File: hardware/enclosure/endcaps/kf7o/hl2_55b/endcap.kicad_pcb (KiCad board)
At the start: 2 copper layers, 106 x 55 mm, 46 parts, among them J2 Male Header, J3 Male Header, J4 Fan, Q1 DTC144E, Q2 IRLML6402, Q3 MULTIFET, Q4 MULTIFET, Q5 MULTIFET, Q6 MULTIFET, Q7 MULTIFET, U1 ACPL-M21L-000E

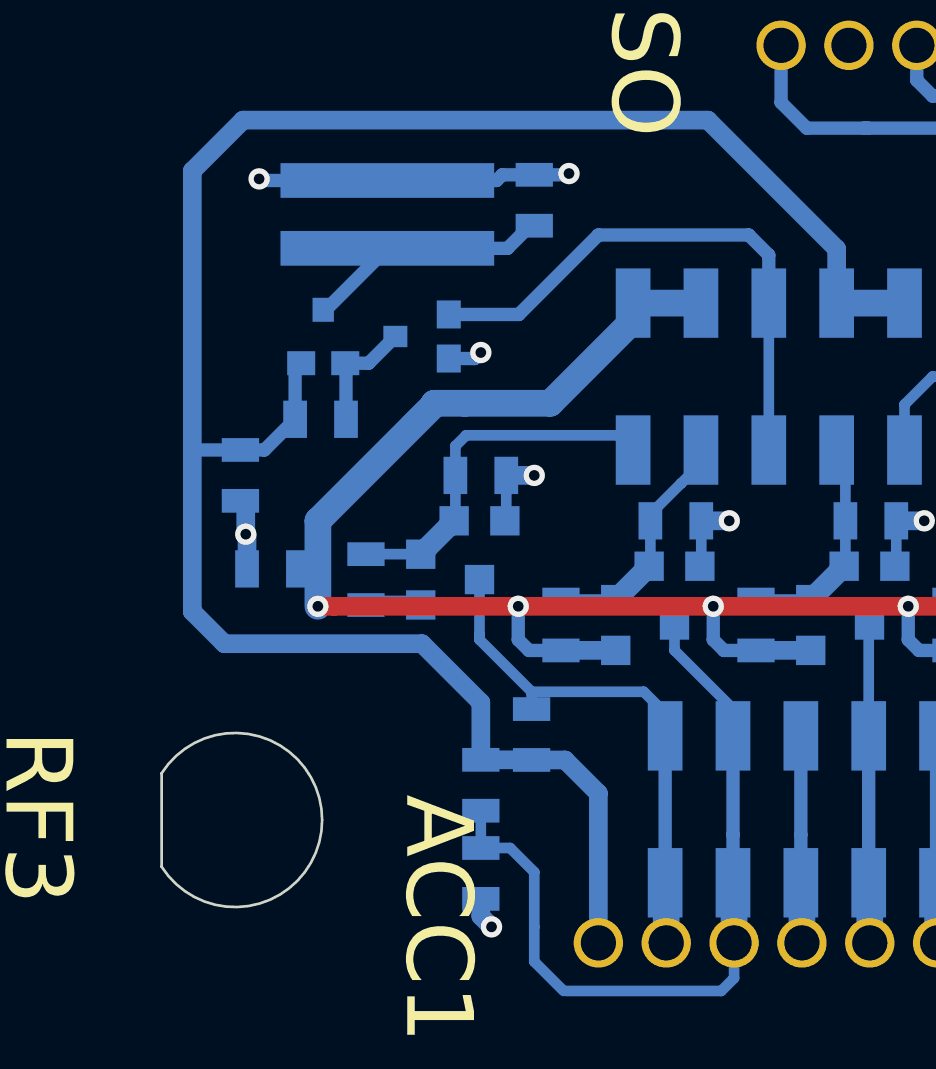
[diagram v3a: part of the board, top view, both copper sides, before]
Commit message: Add LPF for fan on latest end plates
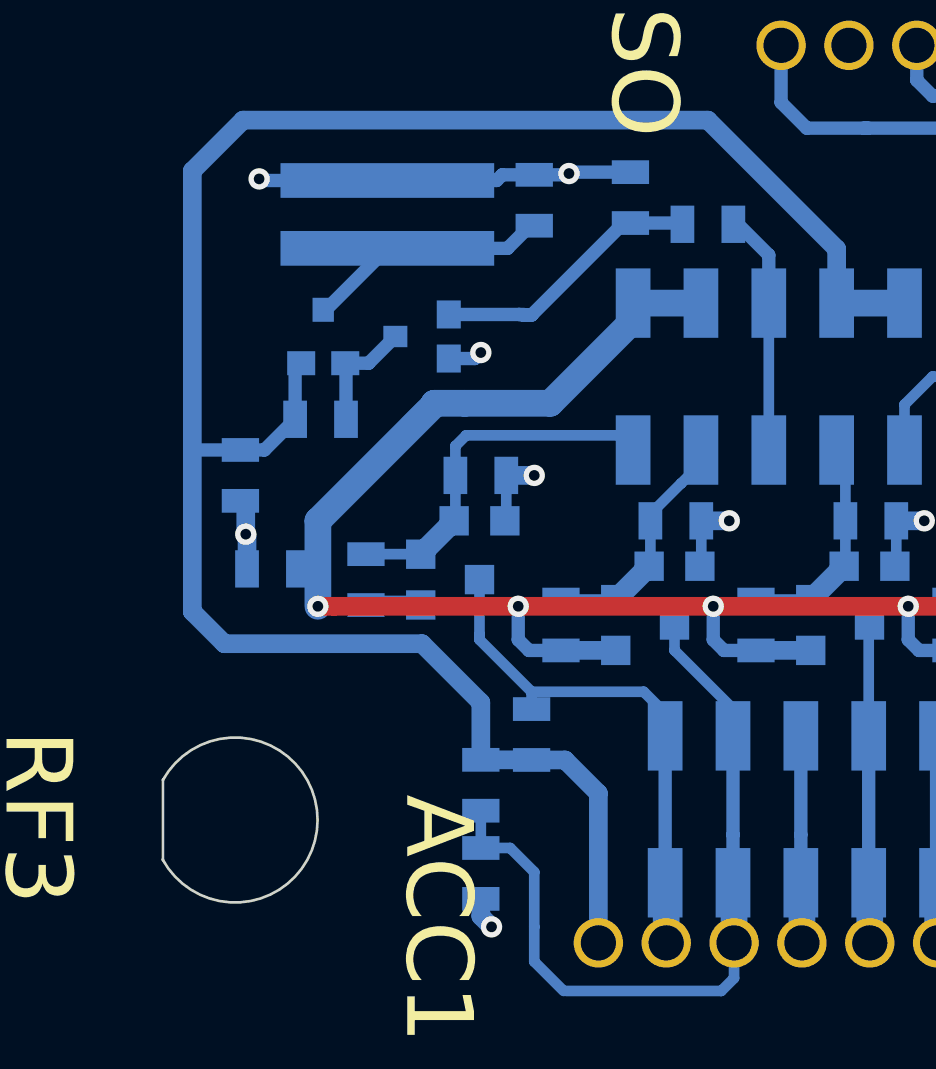
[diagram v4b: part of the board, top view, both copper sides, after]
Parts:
- added C5: 0.1uF, endcaplib:SMD-0805, B.Cu at (94.2, 71.6)
- added R18: 1K, endcaplib:SMD-0805, B.Cu at (97.1, 72.6)
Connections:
- Q1 pad 1: Net-(J2-Pad5) -> Net-(C5-Pad2)
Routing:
- net Net-(J2-Pad5): track 21.5 -> 9.75 mm
- net Net-(C5-Pad2): track 0.00 -> 10.7 mm
- net GNDS: track 47.5 -> 49.9 mm
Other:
- board text added: "HL2 IO End Plate v2.1 © 2020 SofterHardware"
- board text removed: "HL2 IO End Plate v2.0 © 2019 SofterHardware"
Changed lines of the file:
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@@
-(kicad_pcb (version 20171130) (host pcbnew 5.0.2-bee76a0~70~ubuntu16.04.1)
+(kicad_pcb (version 20171130) (host pcbnew 5.1.5-52549c5~84~ubuntu18.04.1)
   (general
     (thickness 1.6)
     (drawings 33)
-    (tracks 288)
+    (tracks 297)
     (zones 0)
-    (modules 46)
-    (nets 29)
+    (modules 48)
+    (nets 30)
   )
   (page USLetter)
   (title_block
     (title "Hermes-Lite End Plate 55")
-    (date 2019-12-01)
-    (rev 2.0)
+    (date 2020-03-17)
+    (rev 2.1)
     (company SofterHardware)
     (comment 1 "KF7O Steve Haynal")
@@
     (zone_45_only no)
     (trace_min 0.2)
-    (segment_width 0.2)
-    (edge_width 0.15)
     (via_size 0.8)
     (via_drill 0.4)
@@
     (uvia_min_size 0.2)
     (uvia_min_drill 0.1)
+    (edge_width 0.15)
+    (segment_width 0.2)
     (pcb_text_width 0.3)
     (pcb_text_size 1.5 1.5)
@@
   (net 27 "Net-(C4-Pad2)")
   (net 28 "Net-(J3-Pad15)")
+  (net 29 "Net-(C5-Pad2)")
   (net_class Default "This is the default net class."
     (clearance 0.2)
@@
     (add_net "Net-(C1-Pad2)")
     (add_net "Net-(C4-Pad2)")
+    (add_net "Net-(C5-Pad2)")
     (add_net "Net-(FB1-Pad1)")
     (add_net "Net-(ISO1-Pad2)")
@@
     (add_net VSUP)
     (add_net Vlvds)
+  )
+  (module endcaplib:sma_panel (layer B.Cu)
+    (at 79.4 94.9)
+    (fp_text reference RF3 (at 0 6.3) (layer B.SilkS)
+      (effects (font (size 1 1) (thickness 0.15)) (justify mirror))
+    )
+    (fp_text value SMA (at 0 -4.25) (layer B.Fab)
+      (effects (font (size 1 1) (thickness 0.15)) (justify mirror))
+    )
+    (fp_arc (start 0 0) (end -2.699999 -1.499999) (angle 302.1346022) (layer Edge.Cuts) (width 0.1))
+    (fp_line (start -2.7 1.5) (end -2.7 -1.5) (layer Edge.Cuts) (width 0.1))
   )
   (module endcaplib:SMD-0805 (layer B.Cu)
@@
   (module endcaplib:male_header (layer B.Cu)
     (at 94.3 78.3 270)
-    (fp_text reference J2 (at -4.6 1.5) (layer B.SilkS)
+    (fp_text reference J2 (at -4.5 1.8) (layer B.SilkS)
       (effects (font (size 0.8 0.8) (thickness 0.1)) (justify mirror))
     )
@@
       (rotate (xyz 0 0 0))
     )
-  )
-  (module endcaplib:sma_panel (layer B.Cu)
-    (at 79.4 94.9)
-    (fp_text reference RF3 (at 0 6.3) (layer B.SilkS)
-      (effects (font (size 1 1) (thickness 0.15)) (justify mirror))
-    )
-    (fp_text value SMA (at 0 -4.25) (layer B.Fab)
-      (effects (font (size 1 1) (thickness 0.15)) (justify mirror))
-    )
-    (fp_line (start -2.75 1.75) (end -2.75 -1.75) (layer Edge.Cuts) (width 0.1))
-    (fp_arc (start 0 0) (end -2.749999 -1.749999) (angle 295.0576154) (layer Edge.Cuts) (width 0.1))
   )
   (module endcaplib:SMD-0805 (layer B.Cu)
@@
     (fp_line (start 1.6 -0.6) (end 1.6 2.6) (layer B.SilkS) (width 0.1))
     (pad 1 smd rect (at -0.825 0 270) (size 1.05 0.9) (layers B.Cu B.Paste B.Mask)
-      (net 5 "Net-(J2-Pad5)"))
+      (net 29 "Net-(C5-Pad2)"))
     (pad 3 smd rect (at 0 2 270) (size 0.8 0.9) (layers B.Cu B.Paste B.Mask)
       (net 26 "Net-(Q1-Pad3)"))
@@
     (at 90.6 71.7 270)
     (attr smd)
-    (fp_text reference C4 (at 0.2 -1.9) (layer B.SilkS)
+    (fp_text reference C4 (at 0 -1.6) (layer B.SilkS)
       (effects (font (size 0.8 0.8) (thickness 0.1)) (justify mirror))
     )
@@
       (xy 0.635 -0.87122) (xy 0.61468 -0.89154) (xy 0.60452 -0.89662)) (layer B.SilkS) (width 0.00254))
   )
-  (gr_text "HL2 IO End Plate v2.0\n© 2019 SofterHardware" (at 146 53.7) (layer B.SilkS)
+  (module endcaplib:SMD-0805 (layer B.Cu)
+    (at 94.2 71.6 270)
+    (attr smd)
+    (fp_text reference C5 (at -1.7 -1.7 180) (layer B.SilkS)
+      (effects (font (size 0.8 0.8) (thickness 0.1)) (justify mirror))
+    )
+    (fp_text value 0.1uF (at 0 -0.381 90) (layer B.SilkS) hide
+      (effects (font (size 0.8 0.8) (thickness 0.1)) (justify mirror))
+    )
+    (fp_line (start 1.524 -0.762) (end 0.508 -0.762) (layer B.SilkS) (width 0.1))
+    (fp_line (start 1.524 0.762) (end 1.524 -0.762) (layer B.SilkS) (width 0.1))
+    (fp_line (start 0.508 0.762) (end 1.524 0.762) (layer B.SilkS) (width 0.1))
+    (fp_line (start -1.524 0.762) (end -0.508 0.762) (layer B.SilkS) (width 0.1))
+    (fp_line (start -1.524 -0.762) (end -1.524 0.762) (layer B.SilkS) (width 0.1))
+    (fp_line (start -0.508 -0.762) (end -1.524 -0.762) (layer B.SilkS) (width 0.1))
+    (pad 2 smd rect (at 0.9525 0 270) (size 0.889 1.397) (layers B.Cu B.Paste B.Mask)
+      (net 29 "Net-(C5-Pad2)"))
+    (pad 1 smd rect (at -0.9525 0 270) (size 0.889 1.397) (layers B.Cu B.Paste B.Mask)
+      (net 1 GNDS))
+    (model smd/chip_cms.wrl
+      (at (xyz 0 0 0))
+      (scale (xyz 0.1 0.1 0.1))
+      (rotate (xyz 0 0 0))
+    )
+  )
+  (module endcaplib:SMD-0805 (layer B.Cu)
+    (at 97.1 72.6 180)
+    (attr smd)
+    (fp_text reference R18 (at -0.1 1.4) (layer B.SilkS)
+      (effects (font (size 0.8 0.8) (thickness 0.1)) (justify mirror))
+    )
+    (fp_text value 1K (at 0 -0.381) (layer B.SilkS) hide
+      (effects (font (size 0.8 0.8) (thickness 0.1)) (justify mirror))
+    )
+    (fp_line (start -0.508 -0.762) (end -1.524 -0.762) (layer B.SilkS) (width 0.1))
+    (fp_line (start -1.524 -0.762) (end -1.524 0.762) (layer B.SilkS) (width 0.1))
+    (fp_line (start -1.524 0.762) (end -0.508 0.762) (layer B.SilkS) (width 0.1))
+    (fp_line (start 0.508 0.762) (end 1.524 0.762) (layer B.SilkS) (width 0.1))
+    (fp_line (start 1.524 0.762) (end 1.524 -0.762) (layer B.SilkS) (width 0.1))
+    (fp_line (start 1.524 -0.762) (end 0.508 -0.762) (layer B.SilkS) (width 0.1))
+    (pad 1 smd rect (at -0.9525 0 180) (size 0.889 1.397) (layers B.Cu B.Paste B.Mask)
+      (net 5 "Net-(J2-Pad5)"))
+    (pad 2 smd rect (at 0.9525 0 180) (size 0.889 1.397) (layers B.Cu B.Paste B.Mask)
+      (net 29 "Net-(C5-Pad2)"))
+    (model smd/chip_cms.wrl
+      (at (xyz 0 0 0))
+      (scale (xyz 0.1 0.1 0.1))
+      (rotate (xyz 0 0 0))
+    )
+  )
+  (gr_text "HL2 IO End Plate v2.1\n© 2020 SofterHardware" (at 146 53.7) (layer B.SilkS)
     (effects (font (size 1 1) (thickness 0.12)) (justify left mirror))
   )
@@
   (segment (start 88.6 98.5) (end 89 98.9) (width 0.7) (layer B.Cu) (net 1))
   (segment (start 88.6 97.8525) (end 88.6 98.5) (width 0.7) (layer B.Cu) (net 1))
+  (segment (start 91.9525 70.6475) (end 91.9 70.7) (width 0.5) (layer B.Cu) (net 1))
+  (segment (start 94.2 70.6475) (end 91.9525 70.6475) (width 0.5) (layer B.Cu) (net 1))
   (segment (start 113.5025 88.55) (end 113.5 88.5525) (width 0.7) (layer B.Cu) (net 2))
   (segment (start 115.55 88.55) (end 113.5025 88.55) (width 0.7) (layer B.Cu) (net 2))
@@
   (segment (start 99.38 81.05) (end 99.38 75.55) (width 0.4) (layer B.Cu) (net 5))
   (segment (start 99.38 75.55) (end 99.38 74.9) (width 0.4) (layer B.Cu) (net 5))
-  (segment (start 90.025 75.975) (end 87.4 75.975) (width 0.5) (layer B.Cu) (net 5))
-  (segment (start 99.38 75.55) (end 99.38 73.75) (width 0.5) (layer B.Cu) (net 5))
-  (segment (start 93 73) (end 90.025 75.975) (width 0.5) (layer B.Cu) (net 5))
-  (segment (start 99.38 73.75) (end 98.63 73) (width 0.5) (layer B.Cu) (net 5))
-  (segment (start 98.63 73) (end 93 73) (width 0.5) (layer B.Cu) (net 5))
+  (segment (start 99.38 73.75) (end 99.38 75.55) (width 0.5) (layer B.Cu) (net 5))
+  (segment (start 98.0525 72.6) (end 98.23 72.6) (width 0.5) (layer B.Cu) (net 5))
+  (segment (start 98.23 72.6) (end 99.38 73.75) (width 0.5) (layer B.Cu) (net 5))
   (segment (start 100.9475 86.6475) (end 100.95 86.65) (width 0.25) (layer B.Cu) (net 6))
   (segment (start 98.9 86.6475) (end 100.9475 86.6475) (width 0.25) (layer B.Cu) (net 6))
@@
   (segment (start 113.7825 92.2525) (end 113.28 91.75) (width 0.4) (layer B.Cu) (net 28))
   (segment (start 117.2 92.2525) (end 113.7825 92.2525) (width 0.4) (layer B.Cu) (net 28))
+  (segment (start 90.025 75.975) (end 87.4 75.975) (width 0.5) (layer B.Cu) (net 29))
+  (segment (start 90.025 75.975) (end 90.225 75.975) (width 0.5) (layer B.Cu) (net 29))
+  (segment (start 94.2 72.5525) (end 93.946 72.5525) (width 0.5) (layer B.Cu) (net 29))
+  (segment (start 90.4985 76) (end 90.2 76) (width 0.5) (layer B.Cu) (net 29))
+  (segment (start 90.025 75.975) (end 90.2 76) (width 0.5) (layer B.Cu) (net 29))
+  (segment (start 93.946 72.5525) (end 90.4985 76) (width 0.5) (layer B.Cu) (net 29))
+  (segment (start 90.2 76) (end 90.525 75.975) (width 0.5) (layer B.Cu) (net 29))
+  (segment (start 96.1 72.5525) (end 96.1475 72.6) (width 0.5) (layer B.Cu) (net 29))
+  (segment (start 94.2 72.5525) (end 96.1 72.5525) (width 0.5) (layer B.Cu) (net 29))
   (zone (net 1) (net_name GNDS) (layer F.Cu) (hatch edge 0.508)
     (connect_pads (clearance 0.3))
